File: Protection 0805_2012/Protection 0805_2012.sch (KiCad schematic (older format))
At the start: 5 parts, among them U5 AP9101CK6, U6 ECH8695R-TL-W

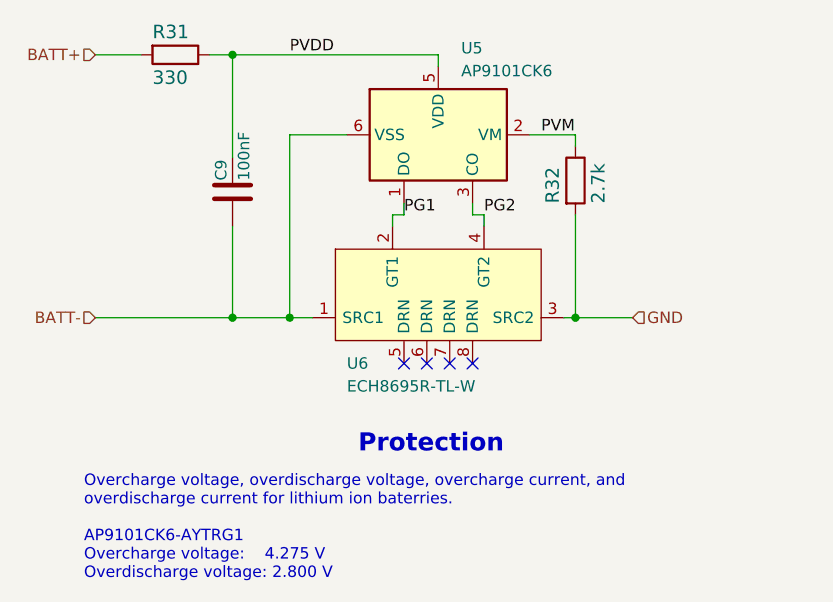
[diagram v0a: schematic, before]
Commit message: Updated Li-Ion schematics
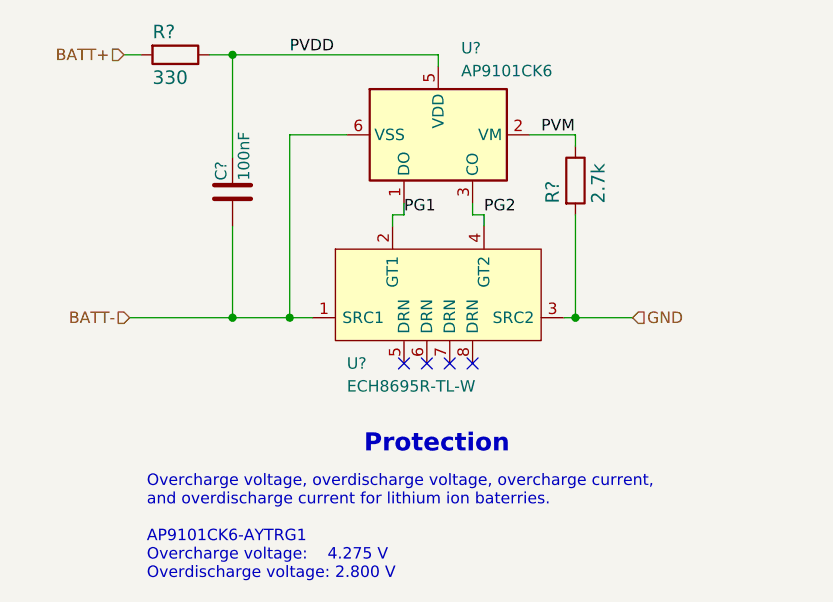
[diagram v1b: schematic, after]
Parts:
- renumbered C9 to C?, R31 to R?, R32 to R?, U5 to U?, U6 to U?
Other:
- note added: "Overcharge voltage, overdischarge voltage, overcharge current, \nand overdischarge current for lithium ion baterries.\n\nAP9101CK6-AYTRG1\nOvercharge voltage: 4.275 V\nOverdischarge voltage: 2.800 V\n"
- note removed: "Overcharge voltage, overdischarge voltage, overcharge current, and\noverdischarge current for lithium ion baterries.\n\nAP9101CK6-AYTRG1\nOvercharge voltage: 4.275 V\nOverdischarge voltage: 2.800 V\n"
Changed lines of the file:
@@
 Comment4 ""
 $EndDescr
-Text Notes 5250 4750 0    79   ~ 16
+Text Notes 5275 4750 0    79   ~ 16
 Protection
 $Comp
-L Li_Ion_LE:AP9101CK6 U5
+L Li_Ion_LE:AP9101CK6 U?
 U 1 1 5EC677B4
 P 5600 3350
-F 0 "U5" H 5700 3700 50  0000 L BNN
+F 0 "U?" H 5700 3700 50  0000 L BNN
 F 1 "AP9101CK6" H 5700 3600 50  0000 L BNN
 F 2 "Li-ion:SOT-23-6" H 5600 3350 50  0001 C CNN
@@
 $EndComp
 $Comp
-L Frequently_Used_LE:R R32
+L Frequently_Used_LE:R R?
 U 1 1 5ECB2DAF
 P 6200 3550
-F 0 "R32" V 6100 3450 59  0000 L CNN
+F 0 "R?" V 6100 3450 59  0000 L CNN
 F 1 "2.7k" V 6300 3450 59  0000 L CNN
 F 2 "Frequently_Used_LE:0805_2012Metric_HandSolder" H 6200 3550 50  0001 C CNN
@@
 $EndComp
 $Comp
-L Li_Ion_LE:ECH8695R-TL-W_Gates_on_Top U6
+L Li_Ion_LE:ECH8695R-TL-W_Gates_on_Top U?
 U 1 1 5ECD5ED5
 P 5600 4050
-F 0 "U6" H 5200 3750 50  0000 L CNN
+F 0 "U?" H 5200 3750 50  0000 L CNN
 F 1 "ECH8695R-TL-W" H 5200 3650 50  0000 L CNN
 F 2 "Li-ion:SOT65P280X95-8N" H 5650 3500 50  0001 C CNN
@@
 	6200 3700 6200 4150
 $Comp
-L Frequently_Used_LE:C C9
+L Frequently_Used_LE:C C?
 U 1 1 5ED1BD18
 P 4700 3600
-F 0 "C9" V 4650 3650 50  0000 L CNN
+F 0 "C?" V 4650 3650 50  0000 L CNN
 F 1 "100nF" V 4750 3650 50  0000 L CNN
 F 2 "Li-ion:0805_2012Metric_HandSolder" H 4738 3450 50  0001 C CNN
@@
 	4700 4150 4950 4150
 $Comp
-L Frequently_Used_LE:R R31
+L Frequently_Used_LE:R R?
 U 1 1 5EC910DA
 P 4450 3000
-F 0 "R31" V 4350 2900 59  0000 L CNN
+F 0 "R?" V 4350 2900 59  0000 L CNN
 F 1 "330" V 4550 2900 59  0000 L CNN
 F 2 "Frequently_Used_LE:0805_2012Metric_HandSolder" H 4450 3000 50  0001 C CNN
@@
 $EndComp
 Wire Wire Line
-	4100 3000 4300 3000
+	4225 3000 4300 3000
 Wire Wire Line
 	4600 3000 4700 3000
@@
 Text Label 5800 3700 0    50   ~ 0
 PG2
-Text Notes 4050 5300 0    50   ~ 0
-Overcharge voltage, overdischarge voltage, overcharge current, and\noverdischarge current for lithium ion baterries.\n\nAP9101CK6-AYTRG1\nOvercharge voltage:    4.275 V\nOverdischarge voltage: 2.800 V\n
-Text HLabel 4100 3000 0    50   Input ~ 0
+Text Notes 4325 5300 0    50   ~ 0
+Overcharge voltage, overdischarge voltage, overcharge current, \nand overdischarge current for lithium ion baterries.\n\nAP9101CK6-AYTRG1\nOvercharge voltage:    4.275 V\nOverdischarge voltage: 2.800 V\n
+Text HLabel 4225 3000 0    50   Input ~ 0
 BATT+
-Text HLabel 4100 4150 0    50   Input ~ 0
+Text HLabel 4250 4150 0    50   Input ~ 0
 BATT-
 Text HLabel 6450 4150 2    50   Input ~ 0
@@
 	6200 4150 6450 4150
 Wire Wire Line
-	4100 4150 4700 4150
+	4250 4150 4700 4150
 $EndSCHEMATC
